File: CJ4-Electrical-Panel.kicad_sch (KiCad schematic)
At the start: 43 parts, among them J1 Conn_01x03, J2 Conn_01x03, J3 Conn_01x03, J4 Conn_01x03, J5 Conn_01x03, J6 Conn_01x03, J7 USB_B_Mini, J8 AVR-ISP-6, U1 ATmega32U4-A, Y1 16MHz

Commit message: Finish routing, add JLCPCB part numbers
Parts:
- C1, C3: JLC (none) -> 0402; LCSC (none) -> C52923
- C10, C2: JLC (none) -> 0402; LCSC (none) -> C15525
- C11, C12, C4, C5, C8, C9: JLC (none) -> 0402; LCSC (none) -> C1525
- C6, C7: JLC (none) -> 0402; LCSC (none) -> C1554
- D1: JLC (none) -> SOD-232F; LCSC (none) -> C2128
- FB1: JLC (none) -> 0805; LCSC (none) -> C1017
- J7: footprint (none) -> CJ4-Electrical-Panel:ZX80-B-5P
- R1, R5: JLC (none) -> 0402; LCSC (none) -> C25744
- R2, R3: JLC (none) -> 0402; LCSC (none) -> C25092
- R4: JLC (none) -> 0402; LCSC (none) -> C11702
- Y1: JLC (none) -> SMD-CRY-3225_4P; LCSC (none) -> C13738
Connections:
- net AVIONICS_DISPATCH: now also U1.26 (PD6); no longer U1.19 (PD1)
- net AVIONICS_ON: now also U1.25 (PD4); no longer U1.18 (PD0)
- net BATTERY_EMER: now also U1.40 (PF1); no longer U1.11 (PB3)
- net BATTERY_ON: now also U1.41 (PF0); no longer U1.10 (PB2)
- net EMERLT_ARMED: now also U1.39 (PF4); no longer U1.30 (PB6)
- net EMERLT_ON: now also U1.38 (PF5); no longer U1.12 (PB7)
- net LGEN_ON: now also U1.37 (PF6); no longer U1.8 (PB0)
- net LGEN_RESET: now also U1.36 (PF7); no longer U1.9 (PB1)
- net MISO: now also U1.11 (PB3)
- net MOSI: now also U1.10 (PB2)
- net RGEN_ON: now also U1.27 (PD7); no longer U1.28 (PB4)
- net RGEN_RESET: now also U1.28 (PB4); no longer U1.29 (PB5)
- net SCK: now also U1.9 (PB1)
- net STBY_ON: now also U1.29 (PB5); no longer U1.31 (PC6)
- net STBY_TEST: now also U1.30 (PB6); no longer U1.32 (PC7)
- net DR+: now reaches J7.3 (D+), R2.1
- net DR-: now reaches J7.2 (D-), R3.1
- net VBUS: now reaches FB1.1, J7.1 (VBUS)
- no-connect marks 14 -> 11
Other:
- moved on the sheet: R1

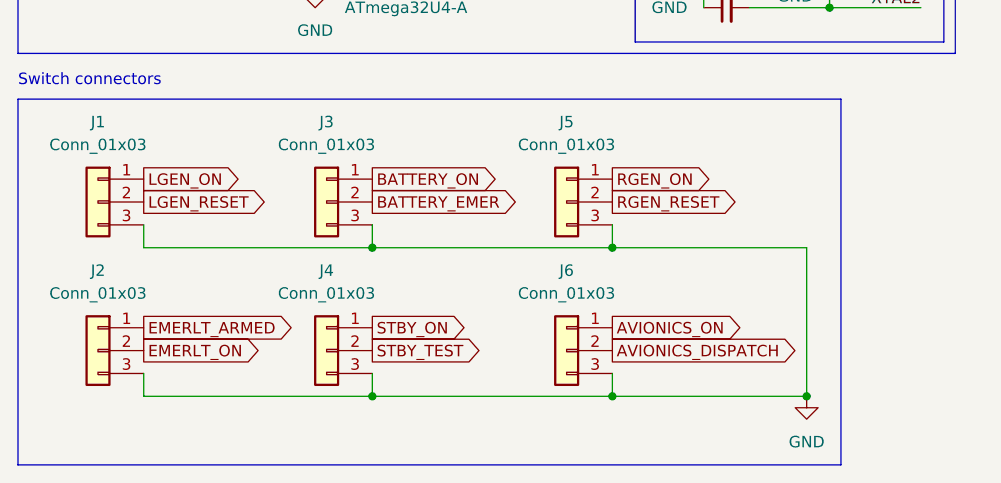
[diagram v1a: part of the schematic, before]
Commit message: Update to KiCad v6 automation
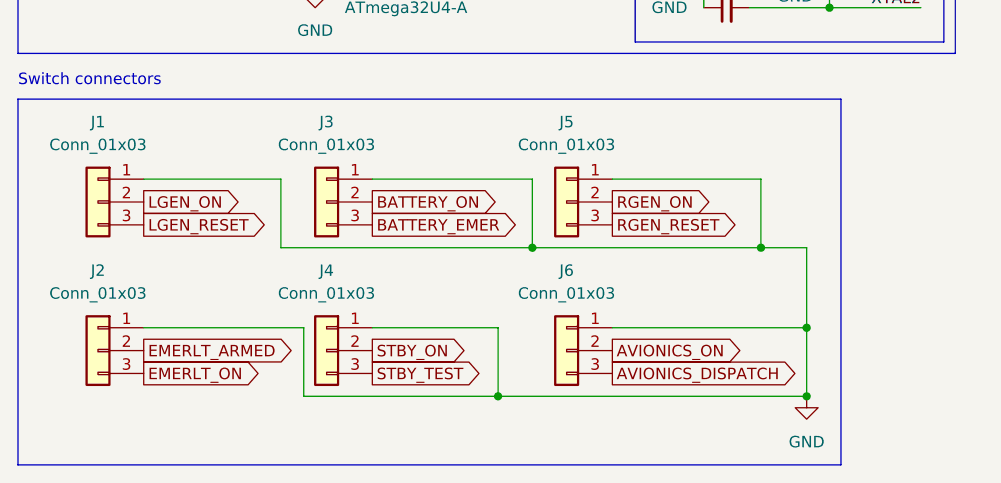
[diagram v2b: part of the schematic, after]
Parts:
- D2, H1, H10, H11, H12, H13, H2, H3, H4, H5, H6, H7, H8, H9, J1, J2, J3, J4, J5, J6, J7, J8, U1: JLC (none) -> DNP
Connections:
- net AVIONICS_DISPATCH: now also J6.3 (Pin_3); no longer J6.2 (Pin_2)
- net AVIONICS_ON: now also J6.2 (Pin_2); no longer J6.1 (Pin_1)
- net BATTERY_EMER: now also J3.3 (Pin_3); no longer J3.2 (Pin_2)
- net BATTERY_ON: now also J3.2 (Pin_2); no longer J3.1 (Pin_1)
- net EMERLT_ARMED: now also J2.2 (Pin_2); no longer J2.1 (Pin_1)
- net EMERLT_ON: now also J2.3 (Pin_3); no longer J2.2 (Pin_2)
- net GND: now also J1.1 (Pin_1), J2.1 (Pin_1), J3.1 (Pin_1), J4.1 (Pin_1), J5.1 (Pin_1), J6.1 (Pin_1); no longer J1.3 (Pin_3), J2.3 (Pin_3), J3.3 (Pin_3), J4.3 (Pin_3), J5.3 (Pin_3), J6.3 (Pin_3)
- net LGEN_ON: now also J1.2 (Pin_2); no longer J1.1 (Pin_1)
- net LGEN_RESET: now also J1.3 (Pin_3); no longer J1.2 (Pin_2)
- net RGEN_ON: now also J5.2 (Pin_2); no longer J5.1 (Pin_1)
- net RGEN_RESET: now also J5.3 (Pin_3); no longer J5.2 (Pin_2)
- net STBY_ON: now also J4.2 (Pin_2); no longer J4.1 (Pin_1)
- net STBY_TEST: now also J4.3 (Pin_3); no longer J4.2 (Pin_2)

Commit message: Add date and version placeholders
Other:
- title: (none) -> CJ4 electrical panel
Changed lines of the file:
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@@
 (kicad_sch (version 20211123) (generator eeschema)
   (paper "A4")
+  (title_block
+    (title "CJ4 electrical panel")
+    (rev "@version@")
+    (comment 1 "Neil Enns")
+    (comment 2 "neile@live.com")
+  )
   (junction (at 95.25 24.13) (diameter 0) (color 0 0 0 0)
   )
